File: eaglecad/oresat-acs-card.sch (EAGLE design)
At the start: 404 parts, among them J2 ORESAT-DEBUG-CONNECTOR-SOLAR, J6 J-SAMTEC-TFM-120-X1-XXX-D-RA, Q10 DMP2240UDM, Q11 MOSFET-PCH-SOT23-6, Q12 MOSFET-PCH-SOT23-6, Q13 PMV45EN, Q14 PMV45EN, Q15 DMP2240UDM, Q21 MOSFET-PCH-SOT23-6, Q22 MOSFET-PCH-SOT23-6, Q23 PMV45EN, Q24 PMV45EN, Q25 DMP2240UDM, Q26 MOSFET-PCH-SOT23-6, Q27 MOSFET-PCH-SOT23-6, Q28 PMV45EN, Q29 PMV45EN, Q30 DMP2240UDM, Q31 MOSFET-PCH-SOT23-6, Q32 MOSFET-PCH-SOT23-6, Q33 PMV45EN, Q34 PMV45EN, Q35 DMP2240UDM, Q6 MOSFET-PCH-SOT23-6, Q7 MOSFET-PCH-SOT23-6, Q8 PMV45EN, Q9 PMV45EN, U1 MAX892LEUA+T21-0036K-L, U10 MAX4211FETE, U11 MIC842LYC5, U12 MIC842LYC5, U13 BMI088, U14 TCAN330, U15 STM32F091C, U17 MAX7310ATE, U18 MAX4211FETE, U19 MIC842LYC5, U2 LTC4300A-1, U20 MIC842LYC5, U25 MAX7310ATE, U26 MAX4211FETE, U27 MIC842LYC5, U28 MIC842LYC5, U29 MAX7310ATE, U30 MAX4211FETE, U31 TPS62111RSA, U32 MIC842LYC5, U33 MIC842LYC5, U5 MAX7310ATE, U6 MAX4211FETE, U7 MIC842LYC5, U8 MIC842LYC5, U9 MAX7310ATE, X2 16MHZ-2.5x2mm

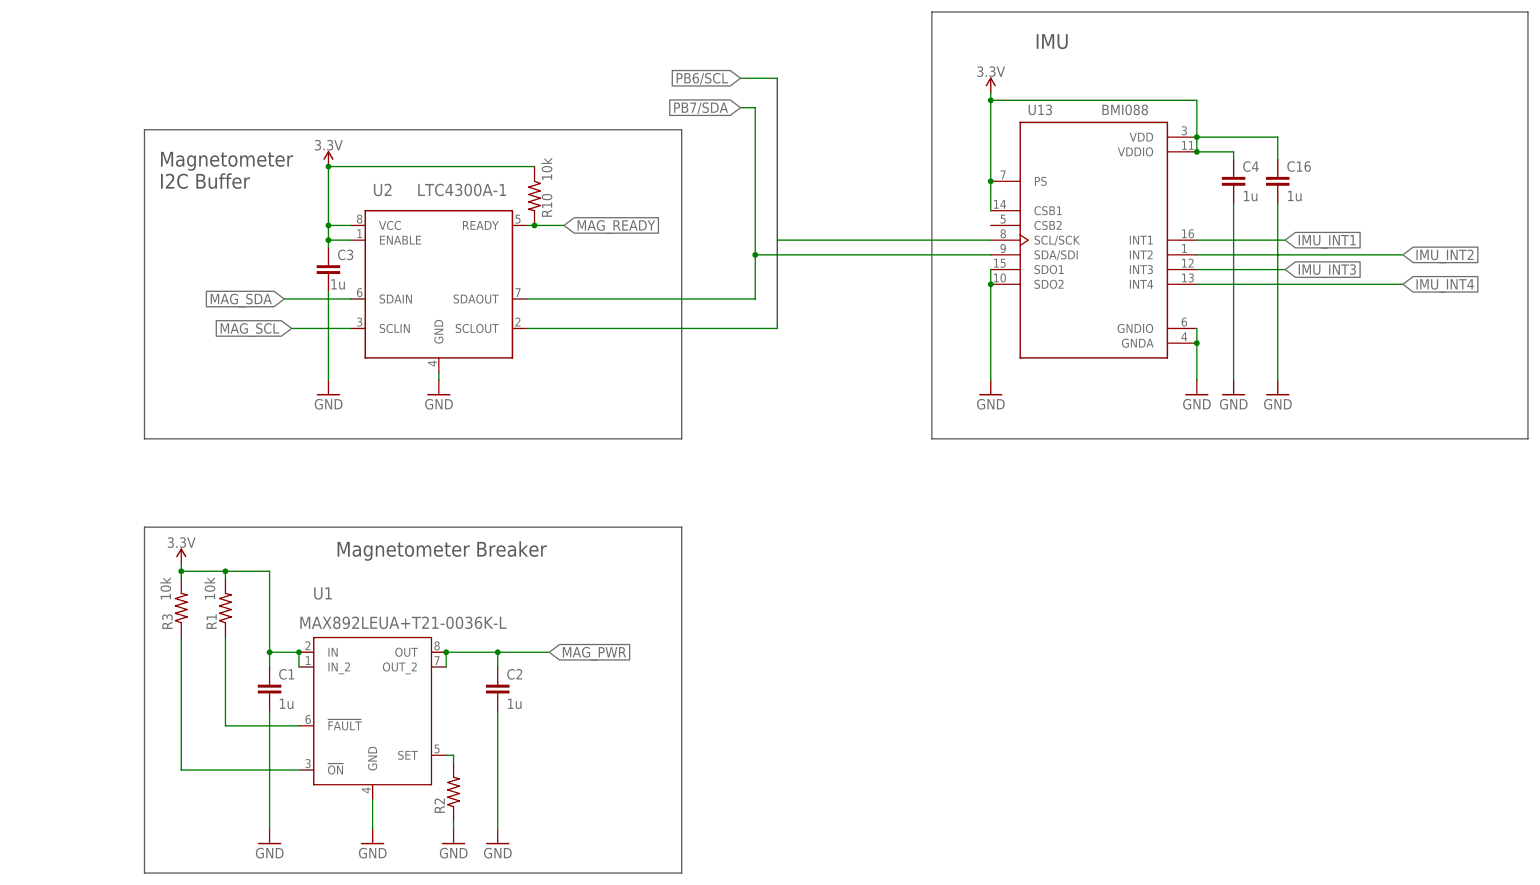
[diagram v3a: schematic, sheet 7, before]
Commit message: Added 10k pull down resistors to SDO pins on IMU. Added labels to magnetometer breaker and value for current set resistor. Removed unused nets connected to the MCU.
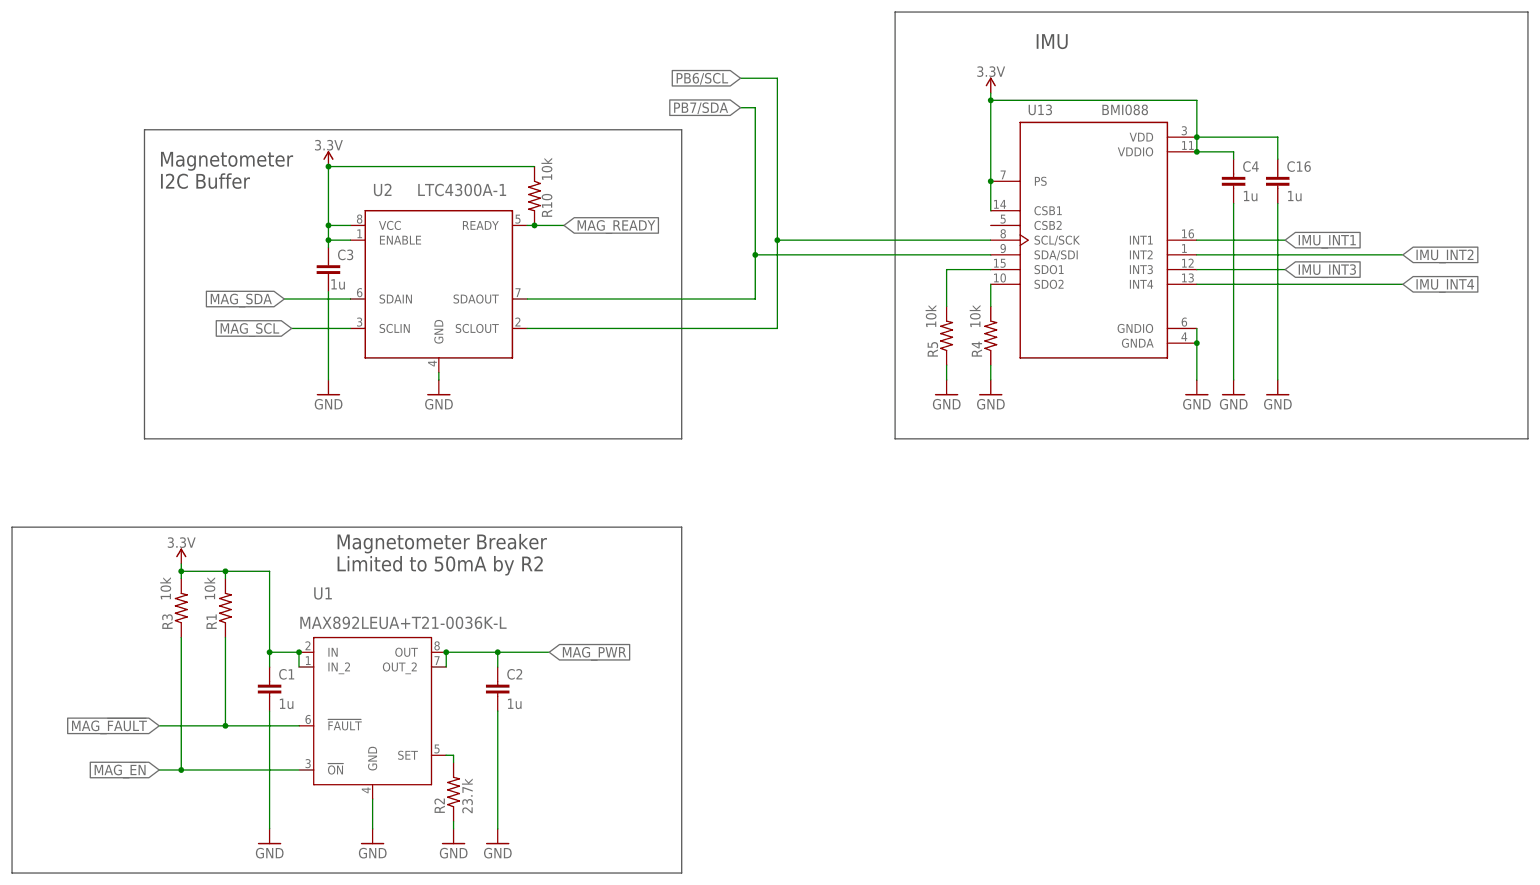
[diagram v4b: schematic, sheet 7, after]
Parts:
- added R4, R5: 10k, oresat-rcl:R-US_0603-C-NOSILK
- R2: value (none) -> 23.7k
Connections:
- removed net PA1: U15.PA1
- removed net PA15: U15.PA15
- removed net PA4: U15.PA4
- removed net PA5/SPI1_SCK: U15.PA5
- removed net PA6/SPI1_MISO: U15.PA6
- removed net PA7/SPI1_MOSI: U15.PA7
- removed net PB0: U15.PB0
- removed net PB1: U15.PB1
- removed net PB10: U15.PB10
- removed net PB11: U15.PB11
- removed net PB2: U15.PB2
- removed net PB8: U15.PB8
- removed net PB9: U15.PB9
- removed net PC13: U15.PC13
- removed net PC14: U15.PC14-OSC32_IN
- removed net PC15: U15.PC15-OSC32_OUT
- new net N$1: R4.2, U13.SDO2
- new net N$24: R5.2, U13.SDO1
- net GND: now also R4.1, R5.1; no longer U13.SDO1, U13.SDO2
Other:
- note added: "Magnetometer Breaker Limited to 50mA by R2"
- note removed: "Magnetometer Breaker"

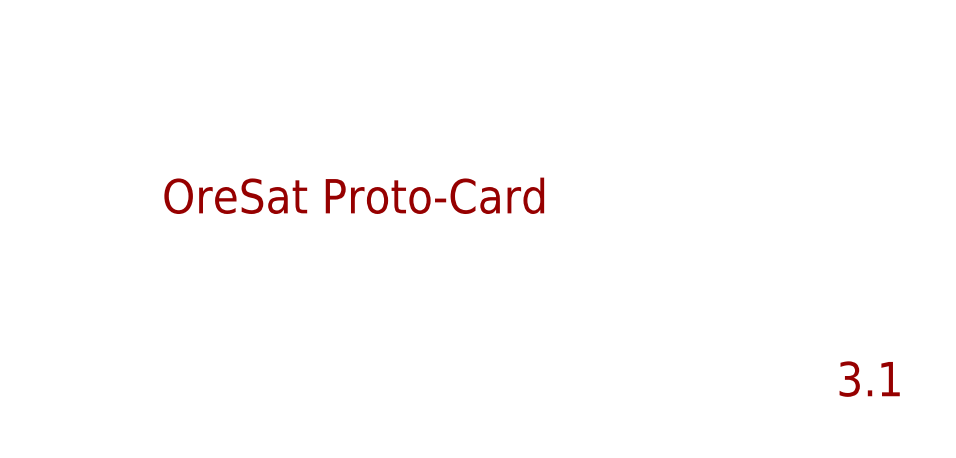
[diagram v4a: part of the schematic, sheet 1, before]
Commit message: Updated name, version number, and date on card and schematic
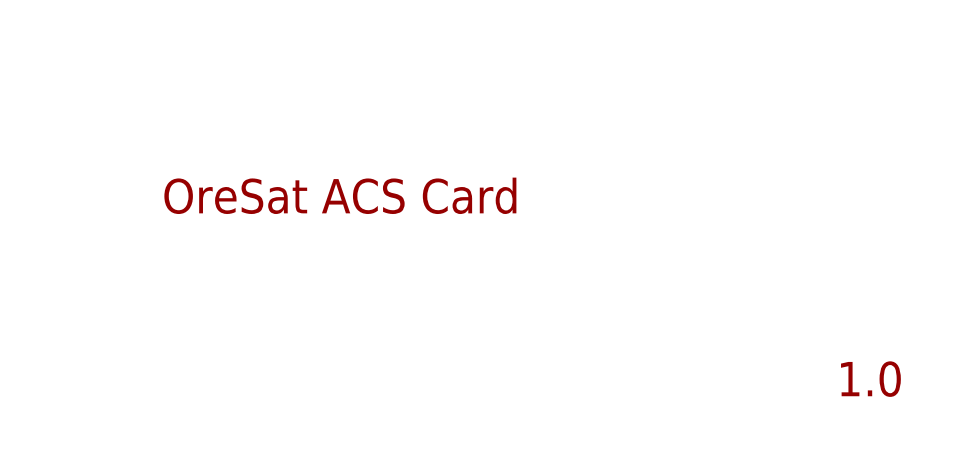
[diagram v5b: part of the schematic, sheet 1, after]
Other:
- note added: "1.0"
- note added: "OreSat ACS Card"
- note removed: "3.1"
- note removed: "OreSat Proto-Card"
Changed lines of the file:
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@@
 <description>Connectors</description>
 <plain>
-<text x="341.63" y="26.67" size="3.81" layer="94">OreSat Proto-Card</text>
-<text x="416.56" y="6.35" size="3.81" layer="94">3.1</text>
+<text x="341.63" y="26.67" size="3.81" layer="94">OreSat ACS Card</text>
+<text x="416.56" y="6.35" size="3.81" layer="94">1.0</text>
 <text x="11.43" y="5.08" size="1.778" layer="97">All resistors 0402 +/- 1% unless marked</text>
 <text x="11.43" y="2.54" size="1.778" layer="97">All caps are 0402 ceramic 10% X5R Vw&gt;=16V unless marked</text>

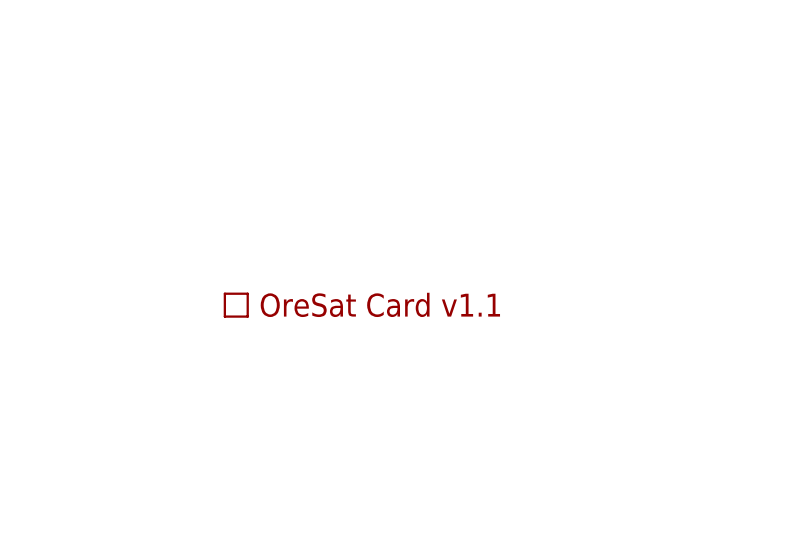
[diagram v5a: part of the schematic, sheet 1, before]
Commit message: Floated BMI088 CSB2 because CSB1 was and data sheet said it had a pull up; switched to card outline with no RF connectors (whoops), moved ground stitching near edges to under TSTOP, fixed some DRC errors because of the stitching move out of TSTOP (I think).
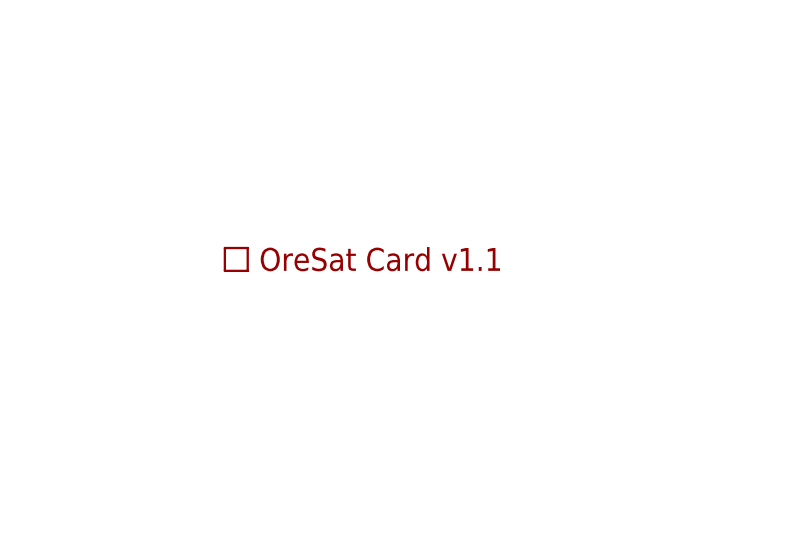
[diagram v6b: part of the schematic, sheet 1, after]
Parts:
- removed U$2: ORESAT-CARD-V1.1-3XRF, oresat-cards:ORESAT-CARD-V1.1-3XRF
- added PCB1: ORESAT-CARD-V1.1-NO-RF, oresat-cards:ORESAT-CARD-V1.1-NO-RF
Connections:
- net 3.3V: no longer U13.CSB1
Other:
- note added: "NC"
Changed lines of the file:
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@@
 <?xml version="1.0" encoding="utf-8"?>
 <!DOCTYPE eagle SYSTEM "eagle.dtd">
-<eagle version="9.5.1">
+<eagle version="9.6.1">
 <drawing>
 <settings>
@@
 </part>
 <part name="GND2" library="supply1" deviceset="GND" device=""/>
-<part name="U$2" library="oresat-cards" deviceset="ORESAT-CARD-V1.1" device="-3XRF"/>
 <part name="QUADRANT1" library="oresat-ACS_driver_board" deviceset="MEZZANINE_PLUG" device=""/>
 <part name="QUADRANT2" library="oresat-ACS_driver_board" deviceset="MEZZANINE_PLUG" device=""/>
@@
 </part>
 <part name="GND13" library="supply1" library_urn="urn:adsk.eagle:library:371" deviceset="GND" device=""/>
+<part name="PCB1" library="oresat-cards" deviceset="ORESAT-CARD-V1.1" device="-NO-RF"/>
 </parts>
 <sheets>
@@
 <attribute name="VALUE" x="139.7" y="100.33" size="1.778" layer="96" rot="MR0"/>
 </instance>
-<instance part="U$2" gate="G$1" x="185.42" y="25.4" smashed="yes"/>
 <instance part="QUADRANT1" gate="G$1" x="279.4" y="205.74" smashed="yes" rot="MR0">
 <attribute name="NAME" x="292.1" y="220.98" size="1.778" layer="95" rot="MR0"/>
@@
 <attribute name="VALUE" x="247.65" y="116.84" size="1.778" layer="96"/>
 </instance>
+<instance part="PCB1" gate="G$1" x="185.42" y="30.48" smashed="yes"/>
 </instances>
 <busses>
@@
 <wire x1="204.47" y1="217.17" x2="204.47" y2="143.51" width="0.1524" layer="97"/>
 <text x="228.6" y="210.82" size="2.54" layer="97">IMU</text>
+<text x="215.9" y="180.34" size="1.778" layer="97">NC</text>
+<text x="215.9" y="182.88" size="1.778" layer="97">NC</text>
 </plain>
 <instances>
@@
 <wire x1="256.54" y1="195.58" x2="270.51" y2="195.58" width="0.1524" layer="91"/>
 <wire x1="270.51" y1="195.58" x2="270.51" y2="191.77" width="0.1524" layer="91"/>
-<pinref part="U13" gate="G$1" pin="CSB1"/>
-<wire x1="220.98" y1="182.88" x2="220.98" y2="187.96" width="0.1524" layer="91"/>
-<junction x="220.98" y="187.96"/>
 </segment>
 <segment>
@@
 for full support of SPICE simulation.
 </note>
+<note version="8.5" severity="warning">
+Since Version 8.5, EAGLE supports locking for holes, vias, wires and polygons.
+The locking property on all objects of these types will not be understood in this version.
+</note>
 </compatibility>
